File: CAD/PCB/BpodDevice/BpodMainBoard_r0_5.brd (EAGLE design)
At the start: 146.3 x 82.2 mm, 43 parts, among them Q3 2N3819, Q4 2N3819

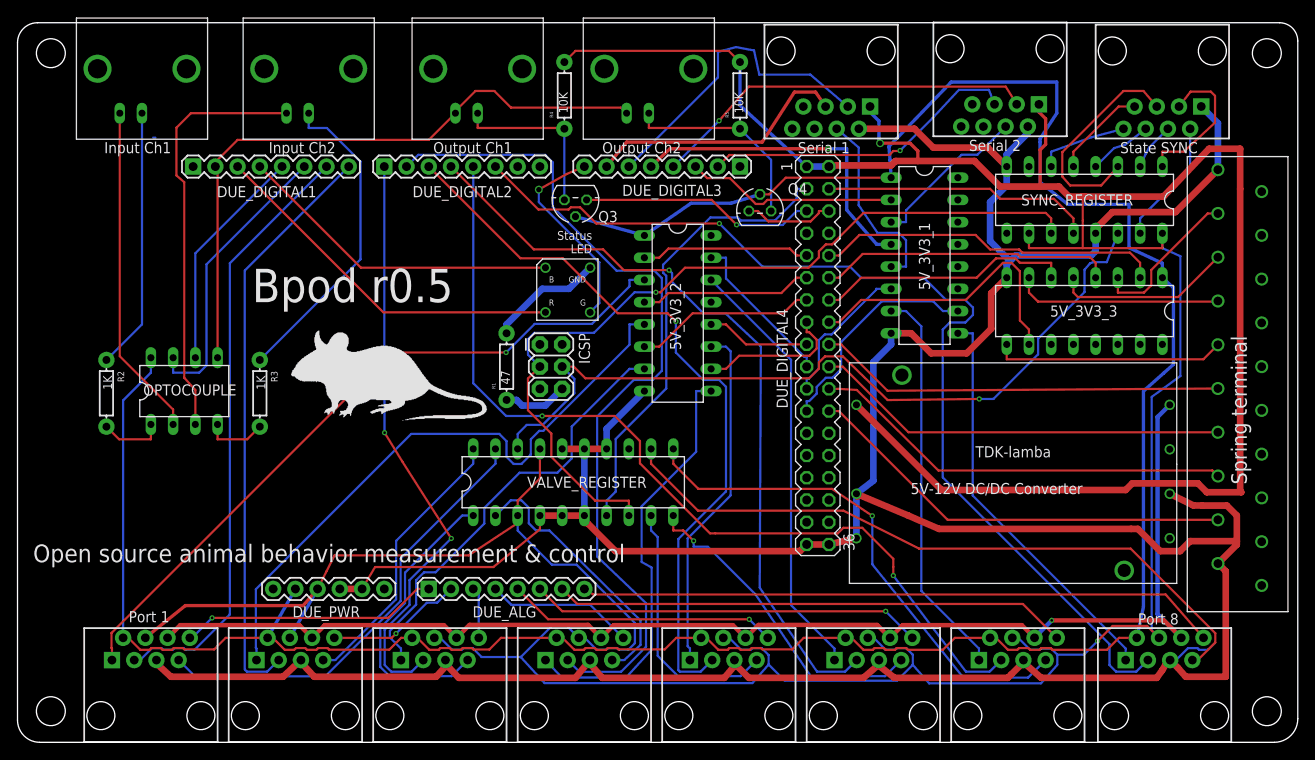
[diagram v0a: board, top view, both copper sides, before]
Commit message: Major update: -Integrates with PsychToolbox (if installed) for low latency serial and possible future use as a sound server -Adds sound support with Teensy Audio board, added as a hardware serial device -Updated to work on Ubuntu 14 with MATLAB r2011a or newer (must create a serial port alias: /dev/TTYACM0 --> /dev/TTYS101) -Added hardware serial override to GUI -Many other bug-fixes
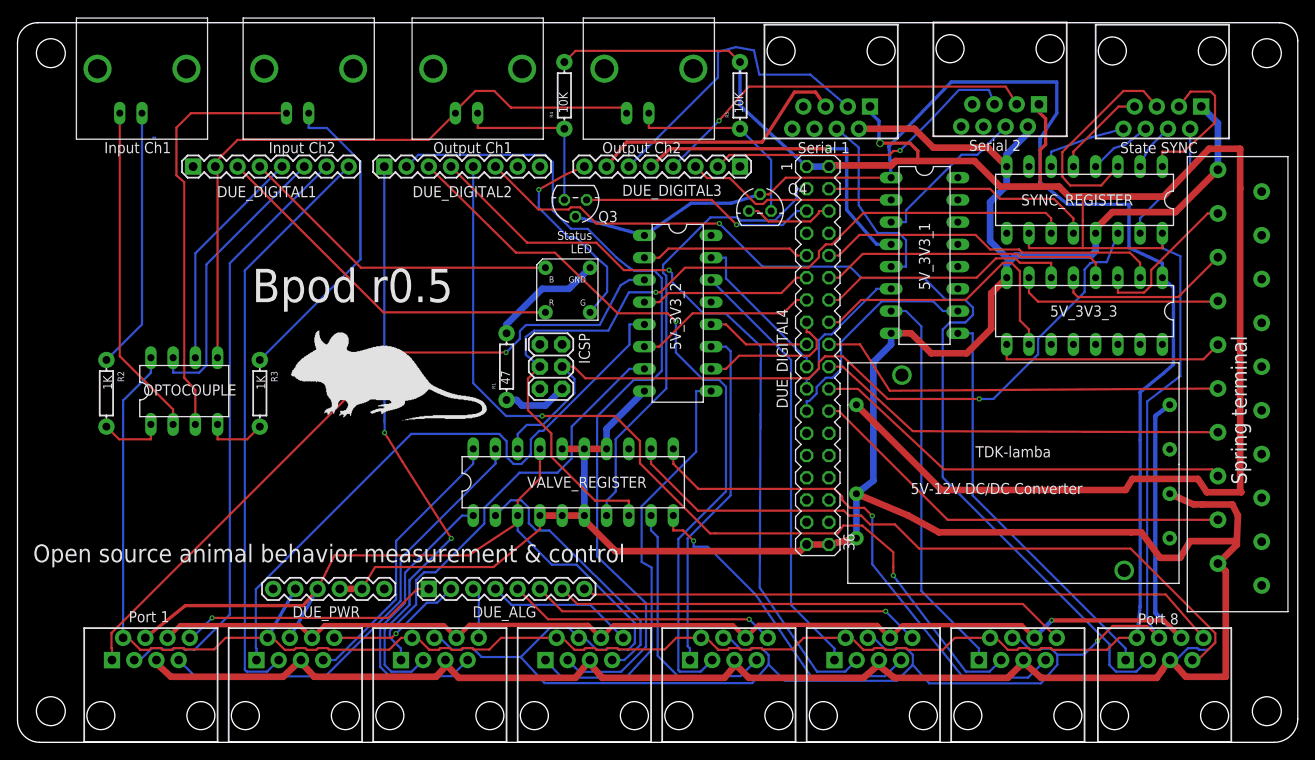
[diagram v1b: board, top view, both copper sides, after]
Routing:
- net GND: track 426.6 -> 428.2 mm
- net SPI_CLK: track 96.5 -> 97.8 mm
- net LED3: track 23.2 -> 24.4 mm
- net 5V: track 488.4 -> 489.5 mm
- net DIGITAL_BUS1: track 81.1 -> 82.0 mm
- net N$16: track 77.9 -> 78.7 mm
- net DSUB_BUS5: track 46.6 -> 47.3 mm
- net LED_BUS7: track 103.3 -> 103.9 mm
- net N$15: track 58.9 -> 59.5 mm

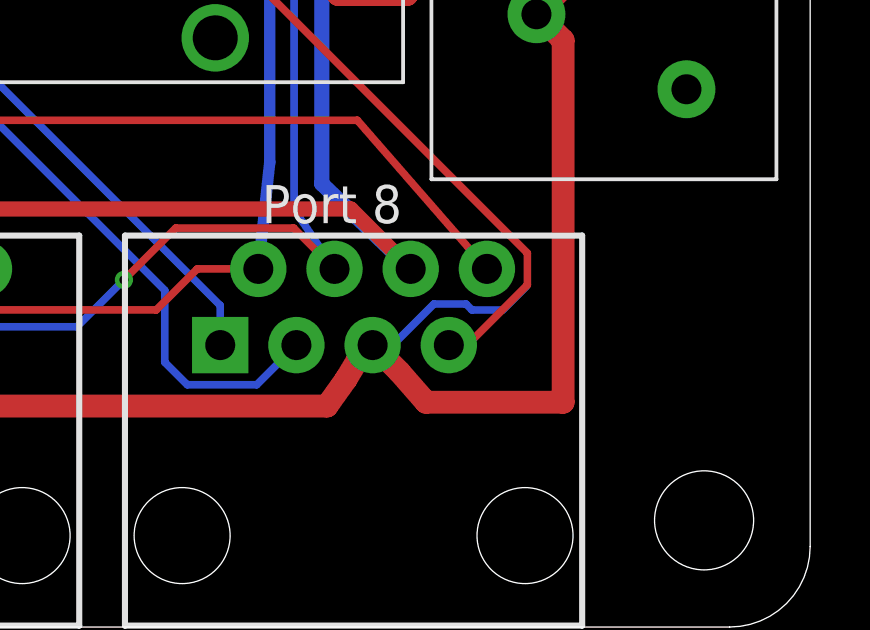
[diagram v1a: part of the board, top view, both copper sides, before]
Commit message: -Fixed bug with override command (crashed if used prior to uploading a state matrix) -Updated PCB design to eliminate a stray trace (did not affect function of prior revision)
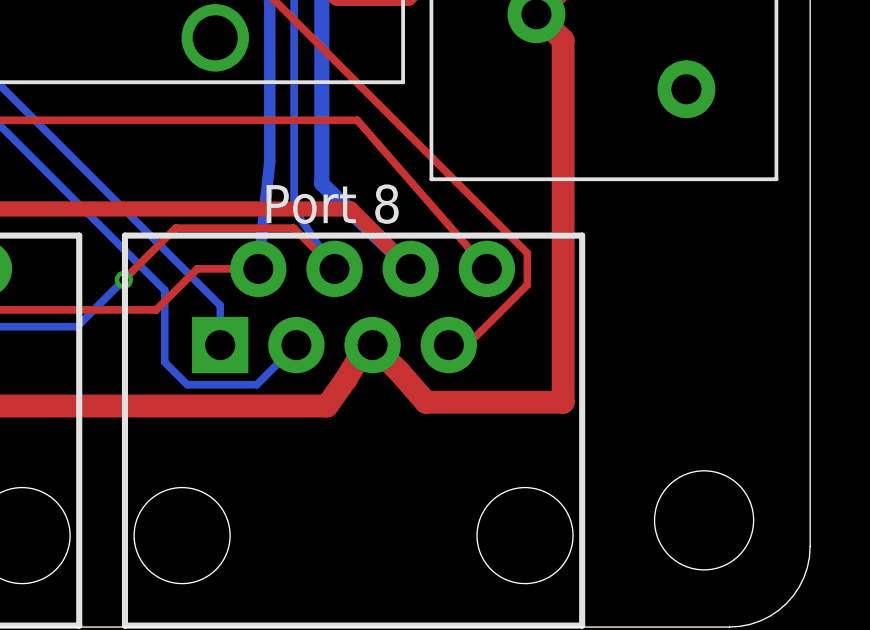
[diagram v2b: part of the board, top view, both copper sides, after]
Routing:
- net GND: track 428.2 -> 422.1 mm
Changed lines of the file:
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@@
 <wire x1="33.0569" y1="9.398" x2="32.385" y2="9.398" width="0.254" layer="16"/>
 <wire x1="64.77" y1="25.908" x2="64.77" y2="25.0571" width="0.254" layer="1"/>
-<wire x1="136.83" y1="11.3638" x2="136.0352" y2="10.569" width="0.254" layer="16"/>
-<wire x1="136.0352" y1="10.569" x2="135.0099" y2="10.569" width="0.254" layer="16"/>
-<wire x1="135.0099" y1="10.569" x2="134.8119" y2="10.767" width="0.254" layer="16"/>
-<wire x1="134.8119" y1="10.767" x2="133.7399" y2="10.767" width="0.254" layer="16"/>
-<wire x1="133.7399" y1="10.767" x2="132.3709" y2="9.398" width="0.254" layer="16"/>
-<wire x1="132.3709" y1="9.398" x2="131.699" y2="9.398" width="0.254" layer="16"/>
 <wire x1="90.17" y1="22.606" x2="92.71" y2="22.606" width="0.762" layer="1"/>
 <wire x1="92.71" y1="22.606" x2="95.854" y2="23.32" width="0.762" layer="1"/>
@@
 <contactref element="PORT8" pad="7"/>
 <wire x1="134.239" y1="9.398" x2="134.8515" y2="9.398" width="0.254" layer="1"/>
-<wire x1="134.8515" y1="9.398" x2="136.8578" y2="11.4043" width="0.254" layer="1"/>
 <wire x1="136.8578" y1="11.4043" x2="136.8578" y2="12.4646" width="0.254" layer="1"/>
 <wire x1="136.8578" y1="12.4646" x2="127.1935" y2="22.1289" width="0.254" layer="1"/>
@@
 <wire x1="97.409" y1="24.892" x2="100.261" y2="24.892" width="0.254" layer="1"/>
 <wire x1="100.261" y1="24.892" x2="103.0241" y2="22.1289" width="0.254" layer="1"/>
+<wire x1="136.8578" y1="11.4043" x2="134.8515" y2="9.398" width="0.254" layer="1"/>
 </signal>
 <signal name="5V">
